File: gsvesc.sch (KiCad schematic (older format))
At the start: 29 parts, among them J1 Conn_01x06, J2 Conn_01x06, J3 Conn_01x06, J4 Conn_01x05, J5 Conn_01x03, J6 USB_B_Mini, J7 BAT+, J8 BAT-

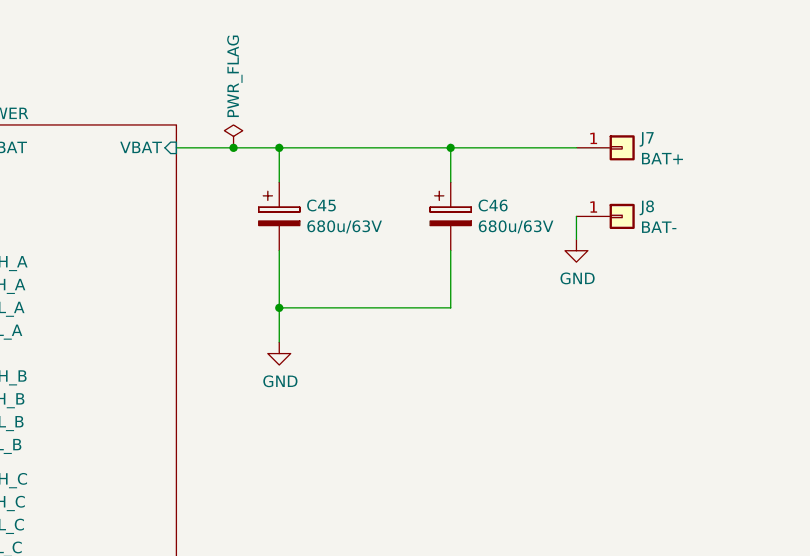
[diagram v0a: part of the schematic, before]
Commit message: Umbau auf doppelFET, INA240
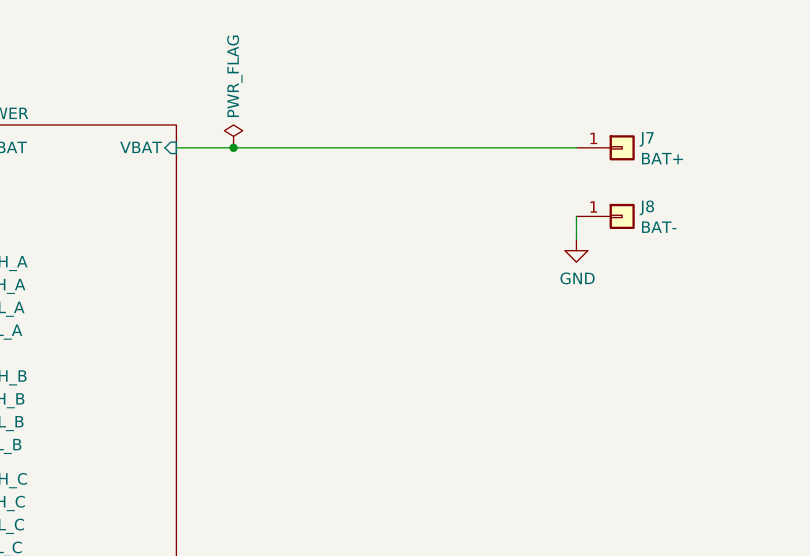
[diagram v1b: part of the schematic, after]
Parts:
- removed C45, C46: 680u/63V, Capacitor_THT:CP_Radial_D12.5mm_P5.00mm, symbol Device:CP
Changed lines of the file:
@@
 	1    0    0    -1
 $EndComp
-Connection ~ 8700 1550
 Wire Wire Line
 	2350 1800 3250 1800
@@
 Wire Wire Line
 	4600 3700 7550 3700
-$Comp
-L power:GND #PWR?
-U 1 1 5DF681DF
-P 8900 2400
-AR Path="/5BECFBCA/5DF681DF" Ref="#PWR?"  Part="1"
-AR Path="/5DF681DF" Ref="#PWR0110"  Part="1"
-F 0 "#PWR0110" H 8900 2150 50  0001 C CNN
-F 1 "GND" H 8905 2227 50  0000 C CNN
-F 2 "" H 8900 2400 50  0001 C CNN
-F 3 "" H 8900 2400 50  0001 C CNN
-	1    8900 2400
-	1    0    0    -1
-$EndComp
-Wire Wire Line
-	8900 2250 8900 2400
-Wire Wire Line
-	8900 2250 9650 2250
-Wire Wire Line
-	9650 2250 9650 2000
-Wire Wire Line
-	8900 2000 8900 2250
-Wire Wire Line
-	8900 1700 8900 1550
-Wire Wire Line
-	9650 1550 9650 1700
-$Comp
-L Device:CP C?
-U 1 1 5DF681EB
-P 9650 1850
-AR Path="/5BECFBCA/5DF681EB" Ref="C?"  Part="1"
-AR Path="/5DF681EB" Ref="C46"  Part="1"
-F 0 "C46" H 9768 1896 50  0000 L CNN
-F 1 "680u/63V" H 9768 1805 50  0000 L CNN
-F 2 "Capacitor_THT:CP_Radial_D12.5mm_P5.00mm" H 9688 1700 50  0001 C CNN
-F 3 "~" H 9650 1850 50  0001 C CNN
-	1    9650 1850
-	1    0    0    -1
-$EndComp
-$Comp
-L Device:CP C?
-U 1 1 5DF681F2
-P 8900 1850
-AR Path="/5BECFBCA/5DF681F2" Ref="C?"  Part="1"
-AR Path="/5DF681F2" Ref="C45"  Part="1"
-F 0 "C45" H 9018 1896 50  0000 L CNN
-F 1 "680u/63V" H 9018 1805 50  0000 L CNN
-F 2 "Capacitor_THT:CP_Radial_D12.5mm_P5.00mm" H 8938 1700 50  0001 C CNN
-F 3 "~" H 8900 1850 50  0001 C CNN
-	1    8900 1850
-	1    0    0    -1
-$EndComp
-Connection ~ 9650 1550
-Wire Wire Line
-	9650 1550 10200 1550
-Connection ~ 8900 2250
-Connection ~ 8900 1550
-Wire Wire Line
-	8900 1550 9650 1550
-Wire Wire Line
-	8700 1550 8900 1550
 Wire Wire Line
 	8450 1550 8700 1550
@@
 Text Notes 7200 7050 0    79   ~ 0
 based on Benjamin Vedders VESC 6
+Wire Wire Line
+	8700 1550 10200 1550
+Connection ~ 8700 1550
 $EndSCHEMATC

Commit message: Version 3 update - JST as SMD part - move FET tracks
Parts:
- J1, J2, J3: footprint Connector_JST:JST_PH_B6B-PH-K_1x06_P2.00mm_Vertical -> Connector_JST:JST_PH_B6B-PH-SM4-TB_1x06-1MP_P2.00mm_Vertical
- J5: footprint Connector_JST:JST_PH_B3B-PH-K_1x03_P2.00mm_Vertical -> Connector_JST:JST_PH_B3B-PH-SM4-TB_1x03-1MP_P2.00mm_Vertical
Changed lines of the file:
@@
 F 0 "J1" H 1420 2725 50  0000 C CNN
 F 1 "Conn_01x06" H 1420 2816 50  0000 C CNN
-F 2 "Connector_JST:JST_PH_B6B-PH-K_1x06_P2.00mm_Vertical" H 1500 3250 50  0001 C CNN
+F 2 "Connector_JST:JST_PH_B6B-PH-SM4-TB_1x06-1MP_P2.00mm_Vertical" H 1500 3250 50  0001 C CNN
 F 3 "~" H 1500 3250 50  0001 C CNN
 	1    1500 3250
@@
 F 0 "J2" H 1420 3925 50  0000 C CNN
 F 1 "Conn_01x06" H 1420 4016 50  0000 C CNN
-F 2 "Connector_JST:JST_PH_B6B-PH-K_1x06_P2.00mm_Vertical" H 1500 4450 50  0001 C CNN
+F 2 "Connector_JST:JST_PH_B6B-PH-SM4-TB_1x06-1MP_P2.00mm_Vertical" H 1500 4450 50  0001 C CNN
 F 3 "~" H 1500 4450 50  0001 C CNN
 	1    1500 4450
@@
 F 0 "J3" H 1420 4775 50  0000 C CNN
 F 1 "Conn_01x06" H 1420 4866 50  0000 C CNN
-F 2 "Connector_JST:JST_PH_B6B-PH-K_1x06_P2.00mm_Vertical" H 1500 5300 50  0001 C CNN
+F 2 "Connector_JST:JST_PH_B6B-PH-SM4-TB_1x06-1MP_P2.00mm_Vertical" H 1500 5300 50  0001 C CNN
 F 3 "~" H 1500 5300 50  0001 C CNN
 	1    1500 5300
@@
 F 0 "J5" H 1420 6525 50  0000 C CNN
 F 1 "Conn_01x03" H 1420 6616 50  0000 C CNN
-F 2 "Connector_JST:JST_PH_B3B-PH-K_1x03_P2.00mm_Vertical" H 1500 6850 50  0001 C CNN
+F 2 "Connector_JST:JST_PH_B3B-PH-SM4-TB_1x03-1MP_P2.00mm_Vertical" H 1500 6850 50  0001 C CNN
 F 3 "~" H 1500 6850 50  0001 C CNN
 	1    1500 6850

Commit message: V3 finish, JLC ready
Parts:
- C1: value 100N -> 100n
- R4: LCSC (none) -> 1
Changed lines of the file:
@@
 F 2 "Resistor_SMD:R_0805_2012Metric" V 2130 2600 50  0001 C CNN
 F 3 "~" H 2200 2600 50  0001 C CNN
+F 4 "1" H 2200 2600 50  0001 C CNN "LCSC"
 	1    2200 2600
 	1    0    0    -1
@@
 P 2800 7050
 F 0 "C1" H 2915 7096 50  0000 L CNN
-F 1 "100N" H 2915 7005 50  0000 L CNN
+F 1 "100n" H 2915 7005 50  0000 L CNN
 F 2 "Capacitor_SMD:C_0805_2012Metric" H 2838 6900 50  0001 C CNN
 F 3 "~" H 2800 7050 50  0001 C CNN

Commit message: V4 first version
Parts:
- added J?: Conn_01x02, symbol Connector_Generic:Conn_01x02
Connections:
- net GND: now also J?.1 (Pin_1)
- net MCU/TEMP_MOTOR: now also J?.2 (Pin_2)
- net POWER/VBAT renamed VBAT
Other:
- note removed: "based on Benjamin Vedders VESC 6"
- moved on the sheet: J7, J8

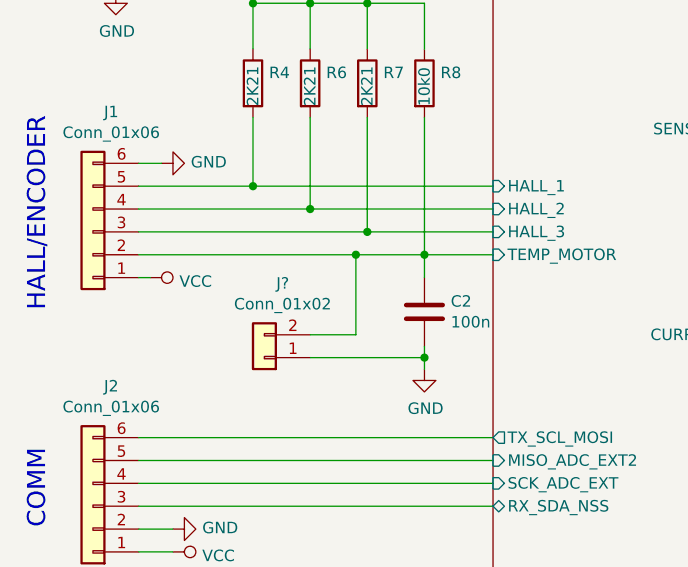
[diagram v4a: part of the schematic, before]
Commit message: Power Supply geändert
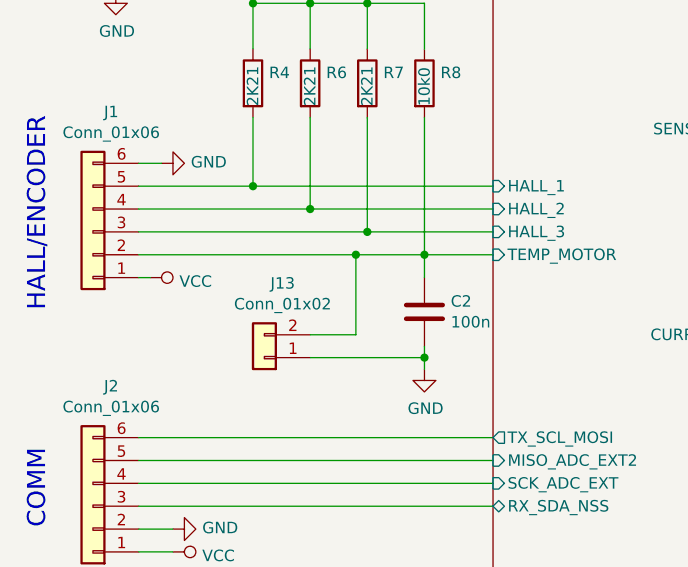
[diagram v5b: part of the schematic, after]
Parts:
- gave numbers to parts that had none: 1
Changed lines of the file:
@@
 	9550 2450 9950 2450
 $Comp
-L power:VCC #PWR?
+L power:VCC #PWR0119
 U 1 1 5E9A7073
 P 9950 2450
-F 0 "#PWR?" H 9950 2300 50  0001 C CNN
+F 0 "#PWR0119" H 9950 2300 50  0001 C CNN
 F 1 "VCC" V 9967 2578 50  0000 L CNN
 F 2 "" H 9950 2450 50  0001 C CNN
@@
 $EndComp
 $Comp
-L power:PWR_FLAG #FLG?
+L power:PWR_FLAG #FLG0101
 U 1 1 5E9A742D
 P 9550 2450
-F 0 "#FLG?" H 9550 2525 50  0001 C CNN
+F 0 "#FLG0101" H 9550 2525 50  0001 C CNN
 F 1 "PWR_FLAG" V 9550 2578 50  0000 L CNN
 F 2 "" H 9550 2450 50  0001 C CNN
@@
 $EndComp
 $Comp
-L power:PWR_FLAG #FLG?
+L power:PWR_FLAG #FLG0103
 U 1 1 5E9A74C6
 P 9550 1900
-F 0 "#FLG?" H 9550 1975 50  0001 C CNN
+F 0 "#FLG0103" H 9550 1975 50  0001 C CNN
 F 1 "PWR_FLAG" V 9550 2028 50  0000 L CNN
 F 2 "" H 9550 1900 50  0001 C CNN
@@
 	9550 2650 9950 2650
 $Comp
-L power:PWR_FLAG #FLG?
+L power:PWR_FLAG #FLG0104
 U 1 1 5E9A754F
 P 9550 2650
-F 0 "#FLG?" H 9550 2725 50  0001 C CNN
+F 0 "#FLG0104" H 9550 2725 50  0001 C CNN
 F 1 "PWR_FLAG" V 9550 2778 50  0000 L CNN
 F 2 "" H 9550 2650 50  0001 C CNN
@@
 	9550 2850 9950 2850
 $Comp
-L power:PWR_FLAG #FLG?
+L power:PWR_FLAG #FLG0105
 U 1 1 5E9AAF43
 P 9550 2850
-F 0 "#FLG?" H 9550 2925 50  0001 C CNN
+F 0 "#FLG0105" H 9550 2925 50  0001 C CNN
 F 1 "PWR_FLAG" V 9550 2978 50  0000 L CNN
 F 2 "" H 9550 2850 50  0001 C CNN
@@
 $EndComp
 $Comp
-L power:+12V #PWR?
+L power:+12V #PWR0120
 U 1 1 5E9AEA9F
 P 9950 2650
-F 0 "#PWR?" H 9950 2500 50  0001 C CNN
+F 0 "#PWR0120" H 9950 2500 50  0001 C CNN
 F 1 "+12V" V 9965 2778 50  0000 L CNN
 F 2 "" H 9950 2650 50  0001 C CNN
@@
 $EndComp
 $Comp
-L power:+5V #PWR?
+L power:+5V #PWR0121
 U 1 1 5E9AEC5A
 P 9950 2850
-F 0 "#PWR?" H 9950 2700 50  0001 C CNN
+F 0 "#PWR0121" H 9950 2700 50  0001 C CNN
 F 1 "+5V" V 9965 2978 50  0000 L CNN
 F 2 "" H 9950 2850 50  0001 C CNN
@@
 $EndComp
 $Comp
-L Connector_Generic:Conn_01x02 J?
+L Connector_Generic:Conn_01x02 J13
 U 1 1 5EC07923
 P 2250 3800
-F 0 "J?" H 2170 3475 50  0000 C CNN
+F 0 "J13" H 2170 3475 50  0000 C CNN
 F 1 "Conn_01x02" H 2170 3566 50  0000 C CNN
 F 2 "" H 2250 3800 50  0001 C CNN

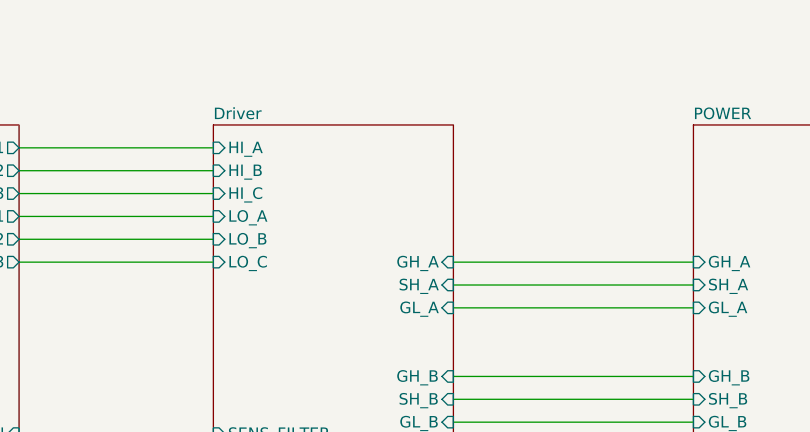
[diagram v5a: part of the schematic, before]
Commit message: Powersupply geändert
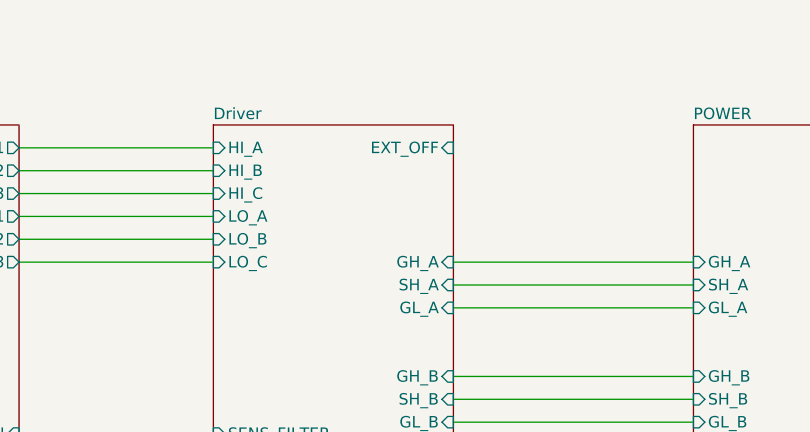
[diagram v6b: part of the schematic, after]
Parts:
- J13: footprint (none) -> Connector_PinHeader_2.54mm:PinHeader_2x01_P2.54mm_Vertical
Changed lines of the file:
@@
 F20 "SENS_B" I L 5450 3100 50
 F21 "SENS_A" I L 5450 3000 50
+F22 "EXT_OFF" I R 6500 1550 50
 $EndSheet
 Wire Wire Line
@@
 F 0 "J13" H 2170 3475 50  0000 C CNN
 F 1 "Conn_01x02" H 2170 3566 50  0000 C CNN
-F 2 "" H 2250 3800 50  0001 C CNN
+F 2 "Connector_PinHeader_2.54mm:PinHeader_2x01_P2.54mm_Vertical" H 2250 3800 50  0001 C CNN
 F 3 "~" H 2250 3800 50  0001 C CNN
 	1    2250 3800

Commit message: V4 pre
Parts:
- J1, J2, J3: footprint Connector_JST:JST_PH_B6B-PH-SM4-TB_1x06-1MP_P2.00mm_Vertical -> Connector_JST:JST_SH_BM06B-SRSS-TB_1x06-1MP_P1.00mm_Vertical
- J13: footprint Connector_PinHeader_2.54mm:PinHeader_2x01_P2.54mm_Vertical -> gsvesc:2pad_smd_testpin
- J5: footprint Connector_JST:JST_PH_B3B-PH-SM4-TB_1x03-1MP_P2.00mm_Vertical -> Connector_JST:JST_SH_BM03B-SRSS-TB_1x03-1MP_P1.00mm_Vertical
- R4, R6, R7: value 2K21 -> 2k70
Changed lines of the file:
@@
 F 0 "J1" H 1420 2725 50  0000 C CNN
 F 1 "Conn_01x06" H 1420 2816 50  0000 C CNN
-F 2 "Connector_JST:JST_PH_B6B-PH-SM4-TB_1x06-1MP_P2.00mm_Vertical" H 1500 3250 50  0001 C CNN
+F 2 "Connector_JST:JST_SH_BM06B-SRSS-TB_1x06-1MP_P1.00mm_Vertical" H 1500 3250 50  0001 C CNN
 F 3 "~" H 1500 3250 50  0001 C CNN
 	1    1500 3250
@@
 F 0 "J2" H 1420 3925 50  0000 C CNN
 F 1 "Conn_01x06" H 1420 4016 50  0000 C CNN
-F 2 "Connector_JST:JST_PH_B6B-PH-SM4-TB_1x06-1MP_P2.00mm_Vertical" H 1500 4450 50  0001 C CNN
+F 2 "Connector_JST:JST_SH_BM06B-SRSS-TB_1x06-1MP_P1.00mm_Vertical" H 1500 4450 50  0001 C CNN
 F 3 "~" H 1500 4450 50  0001 C CNN
 	1    1500 4450
@@
 F 0 "J3" H 1420 4775 50  0000 C CNN
 F 1 "Conn_01x06" H 1420 4866 50  0000 C CNN
-F 2 "Connector_JST:JST_PH_B6B-PH-SM4-TB_1x06-1MP_P2.00mm_Vertical" H 1500 5300 50  0001 C CNN
+F 2 "Connector_JST:JST_SH_BM06B-SRSS-TB_1x06-1MP_P1.00mm_Vertical" H 1500 5300 50  0001 C CNN
 F 3 "~" H 1500 5300 50  0001 C CNN
 	1    1500 5300
@@
 F 0 "J5" H 1420 6525 50  0000 C CNN
 F 1 "Conn_01x03" H 1420 6616 50  0000 C CNN
-F 2 "Connector_JST:JST_PH_B3B-PH-SM4-TB_1x03-1MP_P2.00mm_Vertical" H 1500 6850 50  0001 C CNN
+F 2 "Connector_JST:JST_SH_BM03B-SRSS-TB_1x03-1MP_P1.00mm_Vertical" H 1500 6850 50  0001 C CNN
 F 3 "~" H 1500 6850 50  0001 C CNN
 	1    1500 6850
@@
 P 2450 2600
 F 0 "R6" H 2520 2646 50  0000 L CNN
-F 1 "2K21" V 2450 2500 50  0000 L CNN
+F 1 "2k70" V 2450 2500 50  0000 L CNN
 F 2 "Resistor_SMD:R_0805_2012Metric" V 2380 2600 50  0001 C CNN
 F 3 "~" H 2450 2600 50  0001 C CNN
@@
 P 2700 2600
 F 0 "R7" H 2770 2646 50  0000 L CNN
-F 1 "2K21" V 2700 2500 50  0000 L CNN
+F 1 "2k70" V 2700 2500 50  0000 L CNN
 F 2 "Resistor_SMD:R_0805_2012Metric" V 2630 2600 50  0001 C CNN
 F 3 "~" H 2700 2600 50  0001 C CNN
@@
 P 2200 2600
 F 0 "R4" H 2270 2646 50  0000 L CNN
-F 1 "2K21" V 2200 2500 50  0000 L CNN
+F 1 "2k70" V 2200 2500 50  0000 L CNN
 F 2 "Resistor_SMD:R_0805_2012Metric" V 2130 2600 50  0001 C CNN
 F 3 "~" H 2200 2600 50  0001 C CNN
@@
 F 0 "J13" H 2170 3475 50  0000 C CNN
 F 1 "Conn_01x02" H 2170 3566 50  0000 C CNN
-F 2 "Connector_PinHeader_2.54mm:PinHeader_2x01_P2.54mm_Vertical" H 2250 3800 50  0001 C CNN
+F 2 "gsvesc:2pad_smd_testpin" H 2250 3800 50  0001 C CNN
 F 3 "~" H 2250 3800 50  0001 C CNN
 	1    2250 3800

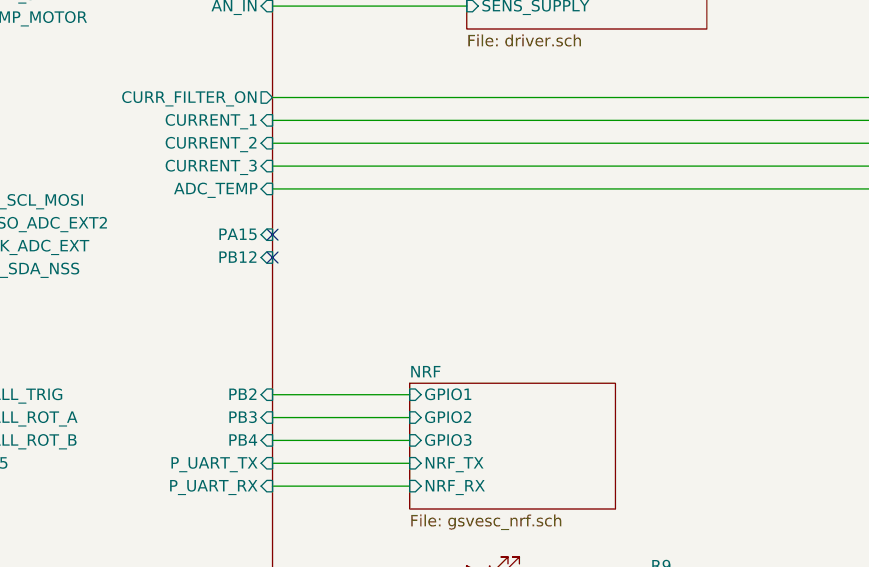
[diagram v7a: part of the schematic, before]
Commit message: Planes und Vias
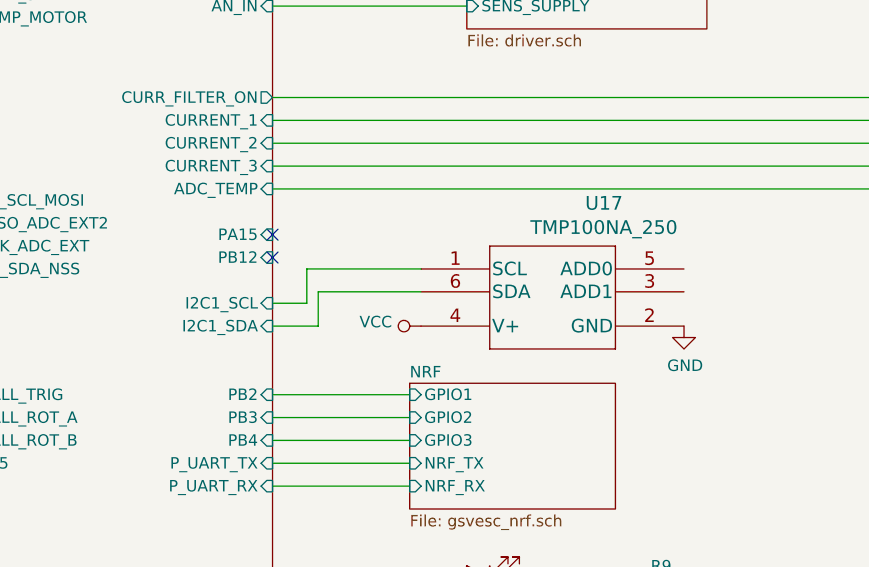
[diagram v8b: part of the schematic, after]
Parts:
- added U17: TMP100NA_250, gsvesc:TMP100NA_250, symbol gsvesc:TMP100NA_250
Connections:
- net GND: now also U17.2 (GND)
- net VCC: now also U17.4 (V+)
- new net MCU/I2C1_SCL: U17.1 (SCL)
- new net MCU/I2C1_SDA: U17.6 (SDA)
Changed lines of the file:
@@
 F43 "CURR_FILTER_ON" O R 4600 3700 50
 F44 "SENS_FILTER_ON" I R 4600 2800 50
+F45 "I2C1_SCL" I R 4600 4600 50
+F46 "I2C1_SDA" I R 4600 4700 50
 $EndSheet
 $Sheet
@@
 	2950 3850 2950 3800
 Connection ~ 2950 3800
+$Comp
+L gsvesc:TMP100NA_250 U17
+U 1 1 5EB0793D
+P 5250 4650
+F 0 "U17" H 6050 5137 60  0000 C CNN
+F 1 "TMP100NA_250" H 6050 5031 60  0000 C CNN
+F 2 "gsvesc:TMP100NA_250" H 6050 4990 60  0001 C CNN
+F 3 "" H 5250 4650 60  0000 C CNN
+	1    5250 4650
+	1    0    0    -1
+$EndComp
+Wire Wire Line
+	4600 4600 4750 4600
+Wire Wire Line
+	4750 4600 4750 4450
+Wire Wire Line
+	4750 4450 5250 4450
+Wire Wire Line
+	4600 4700 4800 4700
+Wire Wire Line
+	4800 4700 4800 4550
+Wire Wire Line
+	4800 4550 5250 4550
+$Comp
+L power:VCC #PWR0159
+U 1 1 5EB10F14
+P 5250 4700
+F 0 "#PWR0159" H 5250 4550 50  0001 C CNN
+F 1 "VCC" V 5268 4827 50  0000 L CNN
+F 2 "" H 5250 4700 50  0001 C CNN
+F 3 "" H 5250 4700 50  0001 C CNN
+	1    5250 4700
+	0    -1   -1   0
+$EndComp
+$Comp
+L power:GND #PWR0160
+U 1 1 5EB11007
+P 6400 4700
+F 0 "#PWR0160" H 6400 4450 50  0001 C CNN
+F 1 "GND" H 6405 4527 50  0000 C CNN
+F 2 "" H 6400 4700 50  0001 C CNN
+F 3 "" H 6400 4700 50  0001 C CNN
+	1    6400 4700
+	1    0    0    -1
+$EndComp
 $EndSCHEMATC
